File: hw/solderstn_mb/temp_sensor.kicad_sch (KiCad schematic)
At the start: 2 parts, among them U901 TMP100

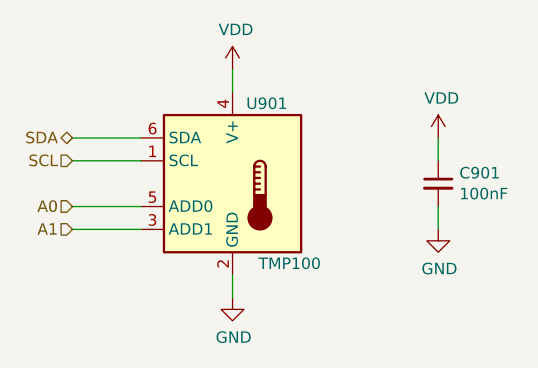
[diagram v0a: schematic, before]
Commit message: solderstn_mb::power - changed generic 2x2 connector to customlib_mj:Molex_MicroFit 2x2
(and a whole bunch of other automatic changes, crap)
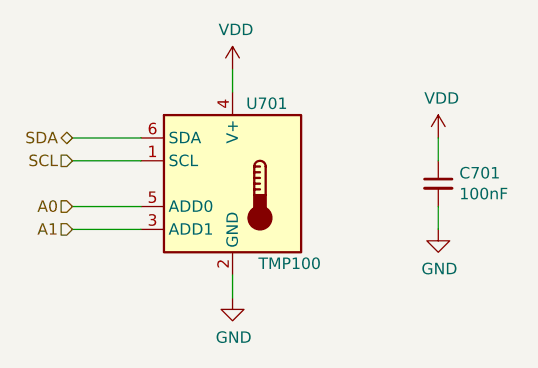
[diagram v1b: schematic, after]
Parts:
- renumbered C901 to C701, U901 to U701
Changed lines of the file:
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@@
     (effects (font (size 1.27 1.27)) (justify right))
   )
-  (symbol (lib_id "power:GND") (at 83.82 72.39 0)
+  (symbol (lib_id "power:GND") (at 83.82 72.39 0) (unit 1)
     (in_bom yes) (on_board yes)
-    (property "Reference" "#PWR0903" (id 0) (at 83.82 78.74 0)
+    (property "Reference" "#PWR0703" (id 0) (at 83.82 78.74 0)
       (effects (font (size 1.27 1.27)) hide)
     )
@@
     (pin "1")
   )
-  (symbol (lib_id "power:VDD") (at 60.96 54.61 0)
+  (symbol (lib_id "power:VDD") (at 60.96 54.61 0) (unit 1)
     (in_bom yes) (on_board yes)
-    (property "Reference" "#PWR0901" (id 0) (at 60.96 58.42 0)
+    (property "Reference" "#PWR0701" (id 0) (at 60.96 58.42 0)
       (effects (font (size 1.27 1.27)) hide)
     )
@@
     (pin "1")
   )
-  (symbol (lib_id "power:VDD") (at 83.82 62.23 0)
+  (symbol (lib_id "power:VDD") (at 83.82 62.23 0) (unit 1)
     (in_bom yes) (on_board yes)
-    (property "Reference" "#PWR0902" (id 0) (at 83.82 66.04 0)
+    (property "Reference" "#PWR0702" (id 0) (at 83.82 66.04 0)
       (effects (font (size 1.27 1.27)) hide)
     )
@@
     (pin "1")
   )
-  (symbol (lib_id "Sensor_Temperature:TMP100") (at 60.96 67.31 0)
+  (symbol (lib_id "Sensor_Temperature:TMP100") (at 60.96 67.31 0) (unit 1)
     (in_bom yes) (on_board yes)
-    (property "Reference" "U901" (id 0) (at 64.77 58.42 0))
+    (property "Reference" "U701" (id 0) (at 64.77 58.42 0))
     (property "Value" "TMP100" (id 1) (at 67.31 76.2 0))
     (property "Footprint" "Package_TO_SOT_SMD:TSOT-23-6" (id 2) (at 60.96 76.2 0)
@@
     (pin "6")
   )
-  (symbol (lib_id "power:GND") (at 60.96 80.01 0)
+  (symbol (lib_id "power:GND") (at 60.96 80.01 0) (unit 1)
     (in_bom yes) (on_board yes)
-    (property "Reference" "#PWR0904" (id 0) (at 60.96 86.36 0)
+    (property "Reference" "#PWR0704" (id 0) (at 60.96 86.36 0)
       (effects (font (size 1.27 1.27)) hide)
     )
@@
     (pin "1")
   )
-  (symbol (lib_id "Device:C_Small") (at 83.82 67.31 0)
+  (symbol (lib_id "Device:C_Small") (at 83.82 67.31 0) (unit 1)
     (in_bom yes) (on_board yes)
-    (property "Reference" "C901" (id 0) (at 86.1568 66.1416 0)
+    (property "Reference" "C701" (id 0) (at 86.1568 66.1416 0)
       (effects (font (size 1.27 1.27)) (justify left))
     )

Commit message: hw: long-standing uncommitted stuff; mostly auto-updates (v7) fw: remove L052 tree (CMSIS & std-HAL shouldn't be committed and it was the wrong device name anyway)
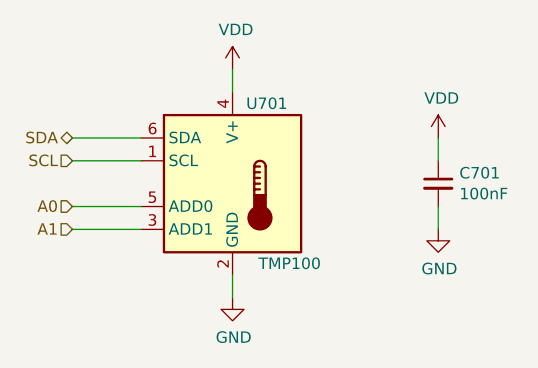
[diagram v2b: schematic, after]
